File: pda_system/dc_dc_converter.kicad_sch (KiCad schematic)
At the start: 15 parts, among them J5 VIN+, J6 GND, J7 VOUT+, J8 GND, U3 MP2307DN_SOIC8N

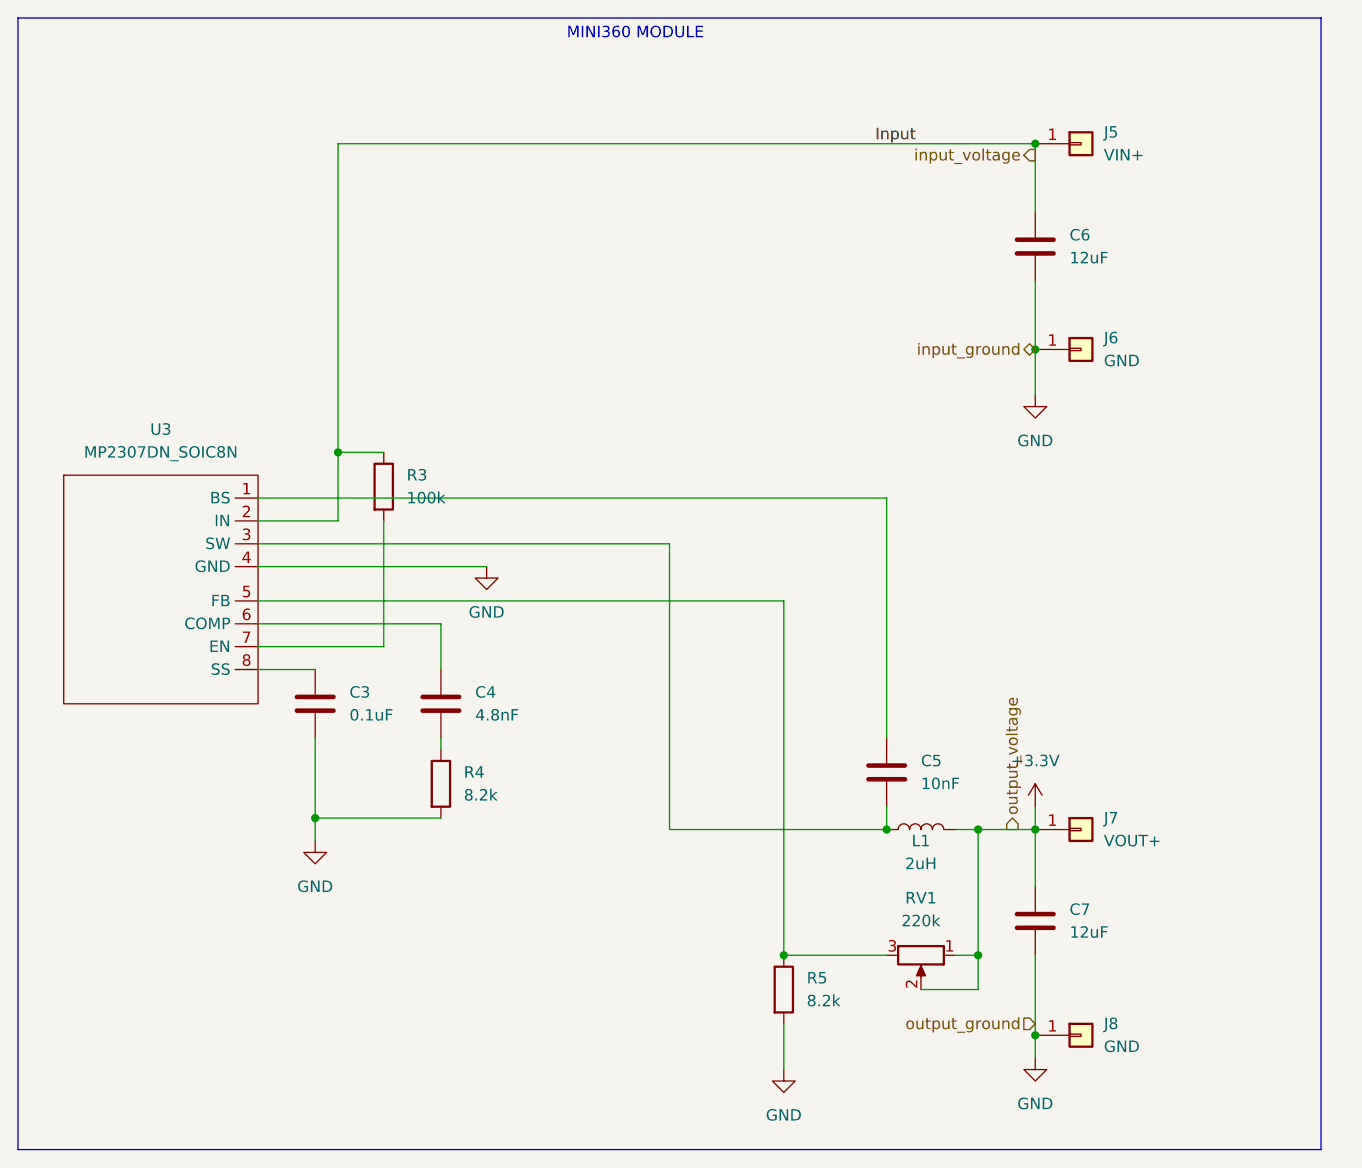
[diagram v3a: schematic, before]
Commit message: minor fixes of ecc issues.
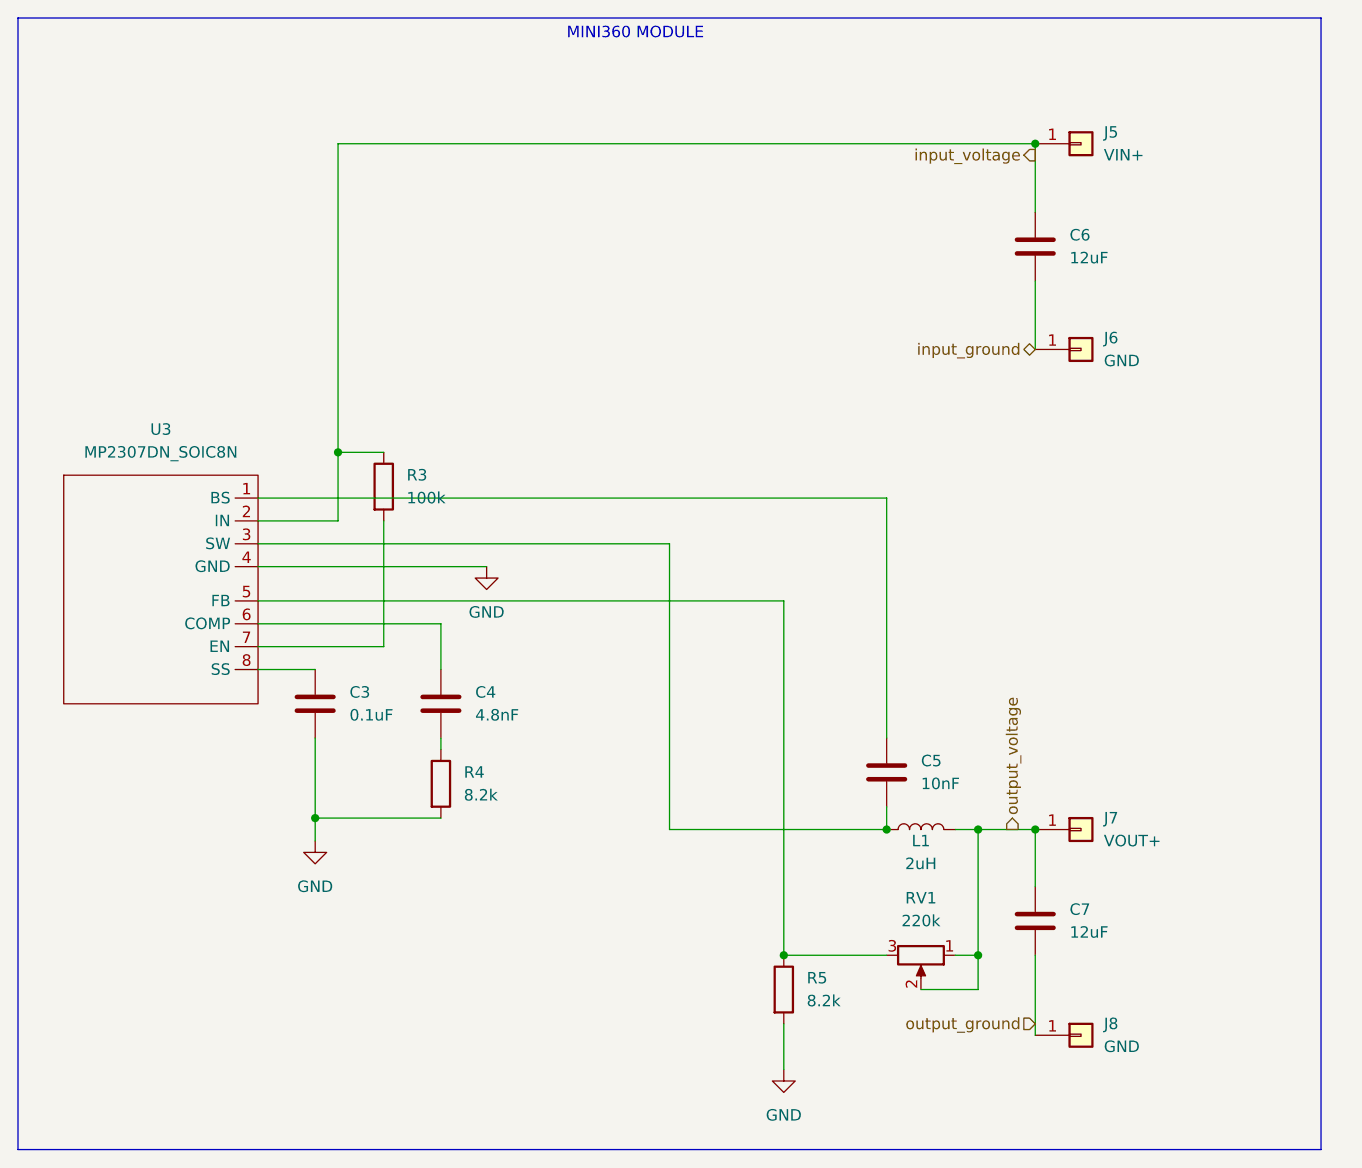
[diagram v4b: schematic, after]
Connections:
- net GND: no longer C6.2, C7.2, J6.1 (Pin_1), J8.1 (Pin_1)
- net +3V3 renamed output_voltage
- new net input_ground: C6.2, J6.1 (Pin_1)
- new net output_ground: C7.2, J8.1 (Pin_1)
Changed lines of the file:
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@@
   (junction (at 53.34 114.3) (diameter 0) (color 0 0 0 0)
   )
-  (junction (at 133.35 138.43) (diameter 0) (color 0 0 0 0)
-  )
-  (junction (at 133.35 62.23) (diameter 0) (color 0 0 0 0)
-  )
   (junction (at 127 129.54) (diameter 0) (color 0 0 0 0)
   )
@@
     (stroke (width 0) (type default) (color 0 0 0 0))
   )
-  (wire (pts (xy 133.35 113.03) (xy 133.35 115.57))
-    (stroke (width 0) (type default) (color 0 0 0 0))
-  )
   (wire (pts (xy 67.31 105.41) (xy 67.31 106.68))
     (stroke (width 0) (type default) (color 0 0 0 0))
@@
     (stroke (width 0) (type default) (color 0 0 0 0))
   )
-  (wire (pts (xy 133.35 62.23) (xy 133.35 67.31))
-    (stroke (width 0) (type default) (color 0 0 0 0))
-  )
   (wire (pts (xy 46.99 81.28) (xy 55.88 81.28))
     (stroke (width 0) (type default) (color 0 0 0 0))
@@
   )
   (wire (pts (xy 124.46 129.54) (xy 127 129.54))
-    (stroke (width 0) (type default) (color 0 0 0 0))
-  )
-  (wire (pts (xy 133.35 138.43) (xy 133.35 140.97))
     (stroke (width 0) (type default) (color 0 0 0 0))
   )
@@
     (effects (font (size 1.27 1.27)) (justify left bottom))
   )
-  (label "Input" (at 115.57 39.37 0)
-    (effects (font (size 1.27 1.27)) (justify left bottom))
-  )
   (hierarchical_label "input_ground" (shape bidirectional) (at 133.35 62.23 180)
     (effects (font (size 1.27 1.27)) (justify right))
@@
     (pin "2")
   )
-  (symbol (lib_id "power:GND") (at 133.35 67.31 0) (unit 1)
-    (in_bom yes) (on_board yes) (fields_autoplaced)
-    (property "Reference" "#PWR0104" (id 0) (at 133.35 73.66 0)
-      (effects (font (size 1.27 1.27)) hide)
-    )
-    (property "Value" "GND" (id 1) (at 133.35 72.39 0))
-    (property "Footprint" "" (id 2) (at 133.35 67.31 0)
-      (effects (font (size 1.27 1.27)) hide)
-    )
-    (property "Datasheet" "" (id 3) (at 133.35 67.31 0)
-      (effects (font (size 1.27 1.27)) hide)
-    )
-    (pin "1")
-  )
   (symbol (lib_id "Device:R") (at 67.31 110.49 0) (unit 1)
     (in_bom yes) (on_board yes) (fields_autoplaced)
@@
     (pin "1")
     (pin "2")
-  )
-  (symbol (lib_id "power:GND") (at 133.35 140.97 0) (unit 1)
-    (in_bom yes) (on_board yes) (fields_autoplaced)
-    (property "Reference" "#PWR0103" (id 0) (at 133.35 147.32 0)
-      (effects (font (size 1.27 1.27)) hide)
-    )
-    (property "Value" "GND" (id 1) (at 133.35 146.05 0))
-    (property "Footprint" "" (id 2) (at 133.35 140.97 0)
-      (effects (font (size 1.27 1.27)) hide)
-    )
-    (property "Datasheet" "" (id 3) (at 133.35 140.97 0)
-      (effects (font (size 1.27 1.27)) hide)
-    )
-    (pin "1")
   )
   (symbol (lib_id "Device:R_Potentiometer") (at 120.65 129.54 270) (unit 1)
@@
       (effects (font (size 1.27 1.27)) hide)
     )
-    (pin "1")
-  )
-  (symbol (lib_id "power:+3.3V") (at 133.35 113.03 0) (unit 1)
-    (in_bom yes) (on_board yes) (fields_autoplaced)
-    (property "Reference" "#PWR0110" (id 0) (at 133.35 116.84 0)
-      (effects (font (size 1.27 1.27)) hide)
-    )
-    (property "Value" "+3.3V" (id 1) (at 133.35 107.95 0))
-    (property "Footprint" "" (id 2) (at 133.35 113.03 0)
-      (effects (font (size 1.27 1.27)) hide)
-    )
-    (property "Datasheet" "" (id 3) (at 133.35 113.03 0)
-      (effects (font (size 1.27 1.27)) hide)
-    )
